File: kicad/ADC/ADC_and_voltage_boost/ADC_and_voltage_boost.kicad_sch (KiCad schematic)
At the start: 10 parts, among them J4 Screw_Terminal_01x02, U3 MOUDLE-SEEEDUINO-XIAO-ESP32C3, U4 MAX1032BEUG_

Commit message: finished schema/pcb
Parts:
- removed C10, C12, C7: 0.1e-6, Capacitor_SMD:C_1206_3216Metric_Pad1.33x1.80mm_HandSolder, symbol Device:C
- removed VoltageBoost1: TPS61023, TerminalBlock_Phoenix:TerminalBlock_Phoenix_MPT-0,5-4-2.54_1x04_P2.54mm_Horizontal, symbol Connector:Screw_Terminal_01x04
- added C1, C2, C3: 0.1e-6, Capacitor_SMD:C_1206_3216Metric_Pad1.33x1.80mm_HandSolder, symbol Device:C
- added J1: Screw_Terminal_01x04, TerminalBlock_Phoenix:TerminalBlock_Phoenix_MPT-0,5-4-2.54_1x04_P2.54mm_Horizontal, symbol Connector:Screw_Terminal_01x04
- J4: footprint (none) -> TerminalBlock_Phoenix:TerminalBlock_Phoenix_MPT-0,5-2-2.54_1x02_P2.54mm_Horizontal
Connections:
- net +3.3V: now also U4.17 (DVDD0), C3.1, J1.1 (Pin_1), J1.4 (Pin_4); no longer C11.1, C11.2, C8.1, C9.1, U3.13 (GND), U4.15 (DGND0), U4.16 (DGND), U4.2 (CH0), U4.21 (AGND3), U4.22 (AVDD2), U4.23 (AGND2), U4.24 (AGND1)
- net +5V: now reaches U4.1 (AVDD1)
- net +5V: now also C11.1, U4.18 (DVDD), U4.2 (CH0), U4.22 (AVDD2), C1.1, C2.1, J1.3 (Pin_3)
- new net GND: C1.2, C11.2, C2.2, C3.2, C8.1, C9.1, J1.2 (Pin_2), U3.13 (GND), U4.15 (DGND0), U4.16 (DGND), U4.21 (AGND3), U4.23 (AGND2), U4.24 (AGND1)
- no-connect marks 0 -> 12

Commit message: updated pcb
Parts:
- removed J4: Screw_Terminal_01x02, TerminalBlock_Phoenix:TerminalBlock_Phoenix_MPT-0,5-2-2.54_1x02_P2.54mm_Horizontal, symbol Connector:Screw_Terminal_01x02
- added J2: Screw_Terminal_01x04, TerminalBlock_Phoenix:TerminalBlock_Phoenix_MPT-0,5-4-2.54_1x04_P2.54mm_Horizontal, symbol Connector:Screw_Terminal_01x04
- C1, C11, C2, C3, C8, C9: footprint Capacitor_SMD:C_1206_3216Metric_Pad1.33x1.80mm_HandSolder -> Capacitor_SMD:C_0805_2012Metric
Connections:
- net GND: now also J2.2 (Pin_2), J2.4 (Pin_4)
- net at U4.3 (CH1): now also J2.3 (Pin_3)
- net at U4.4 (CH2): now also J2.1 (Pin_1)
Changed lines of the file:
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@@
+	)
+	(junction
+		(at 88.9 118.11)
+		(diameter 0)
+		(color 0 0 0 0)
 	)
 	(junction
@@
 	(wire
 		(pts
+			(xy 83.82 118.11) (xy 88.9 118.11)
+		)
+		(stroke
+			(width 0)
+			(type default)
+		)
+	)
+	(wire
+		(pts
 			(xy 161.29 87.63) (xy 191.77 87.63)
 		)
@@
 	(wire
 		(pts
+			(xy 88.9 118.11) (xy 88.9 127)
+		)
+		(stroke
+			(width 0)
+			(type default)
+		)
+	)
+	(wire
+		(pts
 			(xy 119.38 85.09) (xy 116.84 85.09)
 		)
@@
 	(wire
 		(pts
+			(xy 83.82 115.57) (xy 92.71 115.57)
+		)
+		(stroke
+			(width 0)
+			(type default)
+		)
+	)
+	(wire
+		(pts
+			(xy 83.82 120.65) (xy 125.73 120.65)
+		)
+		(stroke
+			(width 0)
+			(type default)
+		)
+	)
+	(wire
+		(pts
 			(xy 113.03 110.49) (xy 113.03 33.02)
 		)
@@
 	(wire
 		(pts
-			(xy 125.73 120.65) (xy 92.71 120.65)
-		)
-		(stroke
-			(width 0)
-			(type default)
-		)
-	)
-	(wire
-		(pts
 			(xy 166.37 74.93) (xy 166.37 92.71)
 		)
@@
 	(wire
 		(pts
+			(xy 83.82 113.03) (xy 88.9 113.03)
+		)
+		(stroke
+			(width 0)
+			(type default)
+		)
+	)
+	(wire
+		(pts
 			(xy 125.73 118.11) (xy 92.71 118.11)
 		)
@@
 	(wire
 		(pts
+			(xy 92.71 118.11) (xy 92.71 115.57)
+		)
+		(stroke
+			(width 0)
+			(type default)
+		)
+	)
+	(wire
+		(pts
 			(xy 119.38 74.93) (xy 166.37 74.93)
+		)
+		(stroke
+			(width 0)
+			(type default)
+		)
+	)
+	(wire
+		(pts
+			(xy 88.9 113.03) (xy 88.9 118.11)
 		)
 		(stroke
@@
 			)
 		)
-		(property "Footprint" "Capacitor_SMD:C_1206_3216Metric_Pad1.33x1.80mm_HandSolder"
+		(property "Footprint" "Capacitor_SMD:C_0805_2012Metric"
 			(at 182.5752 97.79 0)
 			(effects
@@
 			)
 		)
-		(property "Footprint" "Capacitor_SMD:C_1206_3216Metric_Pad1.33x1.80mm_HandSolder"
+		(property "Footprint" "Capacitor_SMD:C_0805_2012Metric"
 			(at 119.6848 140.97 0)
 			(effects
@@
 	)
 	(symbol
+		(lib_id "Connector:Screw_Terminal_01x04")
+		(at 78.74 118.11 180)
+		(unit 1)
+		(exclude_from_sim no)
+		(in_bom yes)
+		(on_board yes)
+		(dnp no)
+		(fields_autoplaced yes)
+		(property "Reference" "J2"
+			(at 78.74 106.68 0)
+			(effects
+				(font
+					(size 1.27 1.27)
+				)
+			)
+		)
+		(property "Value" "Screw_Terminal_01x04"
+			(at 78.74 109.22 0)
+			(effects
+				(font
+					(size 1.27 1.27)
+				)
+			)
+		)
+		(property "Footprint" "TerminalBlock_Phoenix:TerminalBlock_Phoenix_MPT-0,5-4-2.54_1x04_P2.54mm_Horizontal"
+			(at 78.74 118.11 0)
+			(effects
+				(font
+					(size 1.27 1.27)
+				)
+				(hide yes)
+			)
+		)
+		(property "Datasheet" "~"
+			(at 78.74 118.11 0)
+			(effects
+				(font
+					(size 1.27 1.27)
+				)
+				(hide yes)
+			)
+		)
+		(property "Description" "Generic screw terminal, single row, 01x04, script generated (kicad-library-utils/schlib/autogen/connector/)"
+			(at 78.74 118.11 0)
+			(effects
+				(font
+					(size 1.27 1.27)
+				)
+				(hide yes)
+			)
+		)
+		(pin "1"
+		)
+		(pin "2"
+		)
+		(pin "3"
+		)
+		(pin "4"
+		)
+		(instances
+			(project "ADC_and_voltage_boost"
+				(path "/47c680de-131f-4b08-bf1d-2ba63acc97af"
+					(reference "J2")
+					(unit 1)
+				)
+			)
+		)
+	)
+	(symbol
 		(lib_id "power:+3.3V")
 		(at 176.53 40.64 0)
@@
 			)
 		)
-		(property "Footprint" "Capacitor_SMD:C_1206_3216Metric_Pad1.33x1.80mm_HandSolder"
+		(property "Footprint" "Capacitor_SMD:C_0805_2012Metric"
 			(at 204.1652 92.71 0)
 			(effects
@@
 			)
 		)
-		(property "Footprint" "Capacitor_SMD:C_1206_3216Metric_Pad1.33x1.80mm_HandSolder"
+		(property "Footprint" "Capacitor_SMD:C_0805_2012Metric"
 			(at 117.8052 92.71 0)
 			(effects
@@
 	)
 	(symbol
-		(lib_id "Connector:Screw_Terminal_01x02")
-		(at 87.63 120.65 180)
-		(unit 1)
-		(exclude_from_sim no)
-		(in_bom yes)
-		(on_board yes)
-		(dnp no)
-		(fields_autoplaced yes)
-		(property "Reference" "J4"
-			(at 87.63 111.76 0)
-			(effects
-				(font
-					(size 1.27 1.27)
-				)
-			)
-		)
-		(property "Value" "Screw_Terminal_01x02"
-			(at 87.63 114.3 0)
-			(effects
-				(font
-					(size 1.27 1.27)
-				)
-			)
-		)
-		(property "Footprint" "TerminalBlock_Phoenix:TerminalBlock_Phoenix_MPT-0,5-2-2.54_1x02_P2.54mm_Horizontal"
-			(at 87.63 120.65 0)
-			(effects
-				(font
-					(size 1.27 1.27)
-				)
-				(hide yes)
-			)
-		)
-		(property "Datasheet" "~"
-			(at 87.63 120.65 0)
-			(effects
-				(font
-					(size 1.27 1.27)
-				)
-				(hide yes)
-			)
-		)
-		(property "Description" "Generic screw terminal, single row, 01x02, script generated (kicad-library-utils/schlib/autogen/connector/)"
-			(at 87.63 120.65 0)
-			(effects
-				(font
-					(size 1.27 1.27)
-				)
-				(hide yes)
-			)
-		)
-		(pin "2"
-		)
-		(pin "1"
-		)
-		(instances
-			(project "ADC_and_voltage_boost"
-				(path "/47c680de-131f-4b08-bf1d-2ba63acc97af"
-					(reference "J4")
-					(unit 1)
-				)
-			)
-		)
-	)
-	(symbol
 		(lib_id "power:+5V")
 		(at 166.37 92.71 270)
@@
 	(symbol
 		(lib_id "power:GND")
+		(at 88.9 127 0)
+		(unit 1)
+		(exclude_from_sim no)
+		(in_bom yes)
+		(on_board yes)
+		(dnp no)
+		(fields_autoplaced yes)
+		(property "Reference" "#PWR012"
+			(at 88.9 133.35 0)
+			(effects
+				(font
+					(size 1.27 1.27)
+				)
+				(hide yes)
+			)
+		)
+		(property "Value" "GND"
+			(at 88.9 132.08 0)
+			(effects
+				(font
+					(size 1.27 1.27)
+				)
+			)
+		)
+		(property "Footprint" ""
+			(at 88.9 127 0)
+			(effects
+				(font
+					(size 1.27 1.27)
+				)
+				(hide yes)
+			)
+		)
+		(property "Datasheet" ""
+			(at 88.9 127 0)
+			(effects
+				(font
+					(size 1.27 1.27)
+				)
+				(hide yes)
+			)
+		)
+		(property "Description" ""
+			(at 88.9 127 0)
+			(effects
+				(font
+					(size 1.27 1.27)
+				)
+			)
+		)
+		(pin "1"
+		)
+		(instances
+			(project "ADC_and_voltage_boost"
+				(path "/47c680de-131f-4b08-bf1d-2ba63acc97af"
+					(reference "#PWR012")
+					(unit 1)
+				)
+			)
+		)
+	)
+	(symbol
+		(lib_id "power:GND")
 		(at 116.84 92.71 0)
 		(unit 1)
@@
 			)
 		)
-		(property "Footprint" "Capacitor_SMD:C_1206_3216Metric_Pad1.33x1.80mm_HandSolder"
+		(property "Footprint" "Capacitor_SMD:C_0805_2012Metric"
 			(at 195.2752 97.79 0)
 			(effects
@@
 			)
 		)
-		(property "Footprint" "Capacitor_SMD:C_1206_3216Metric_Pad1.33x1.80mm_HandSolder"
+		(property "Footprint" "Capacitor_SMD:C_0805_2012Metric"
 			(at 122.2248 132.08 0)
 			(effects

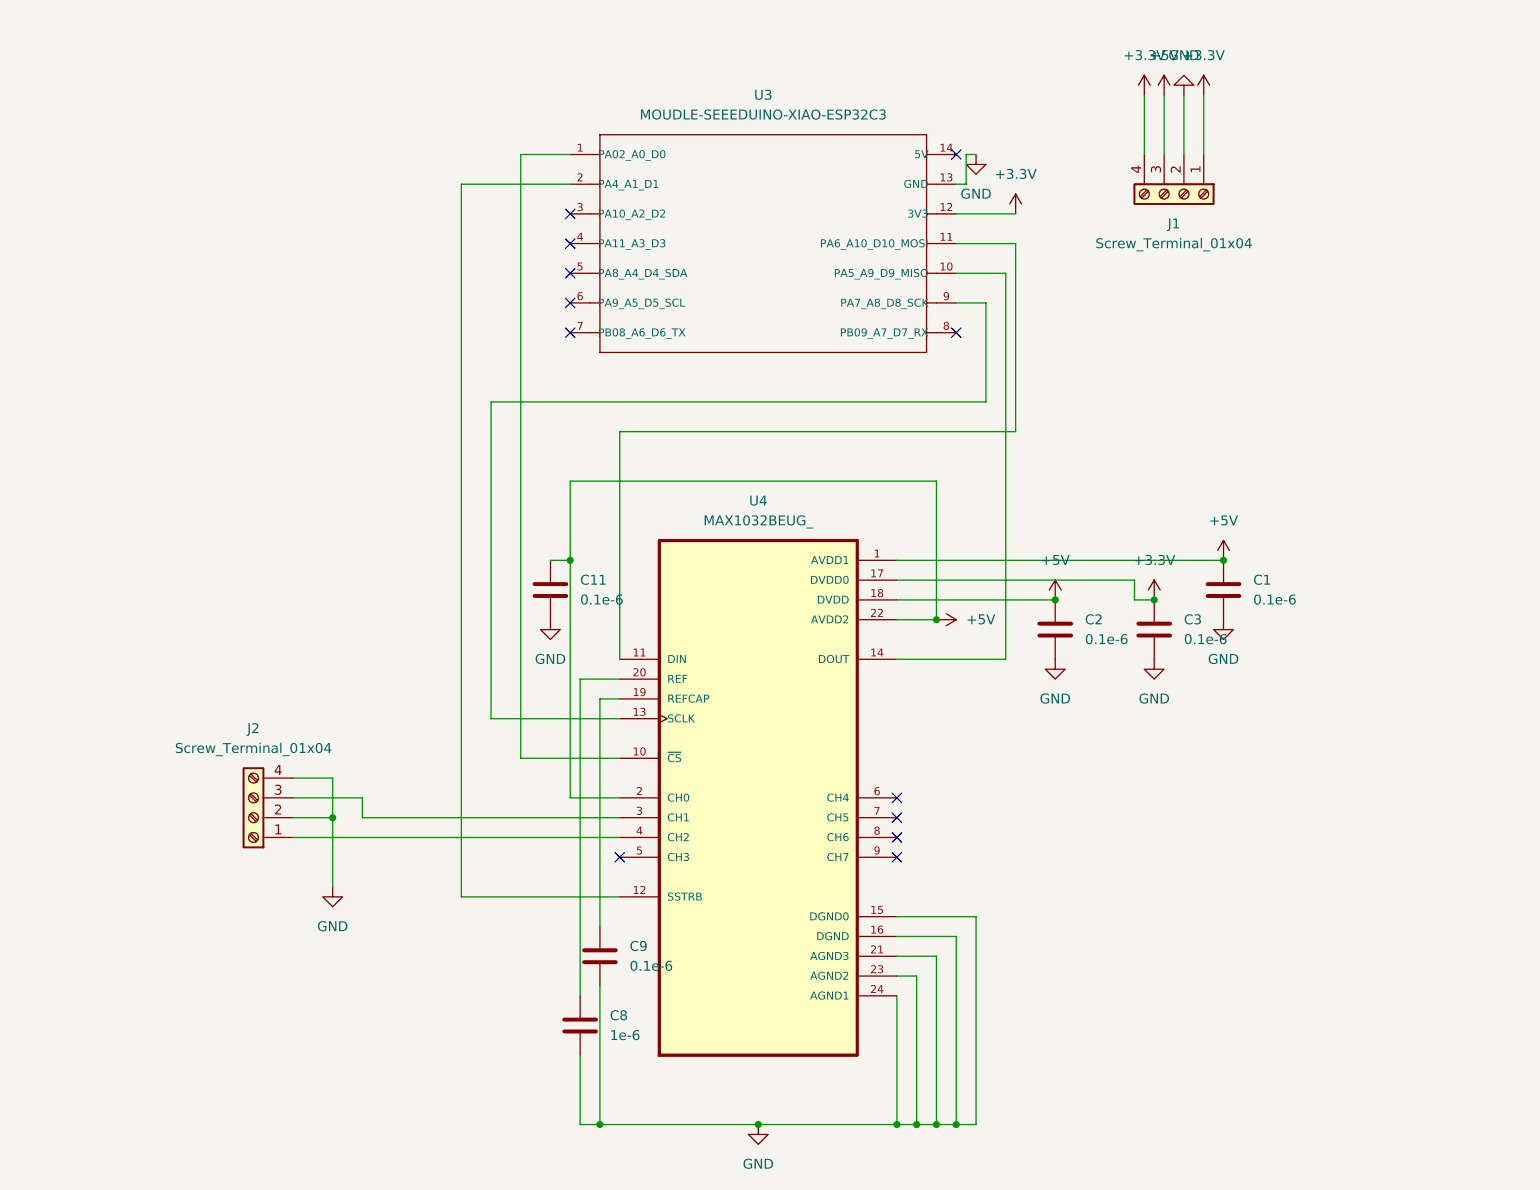
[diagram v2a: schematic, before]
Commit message: finished ADC
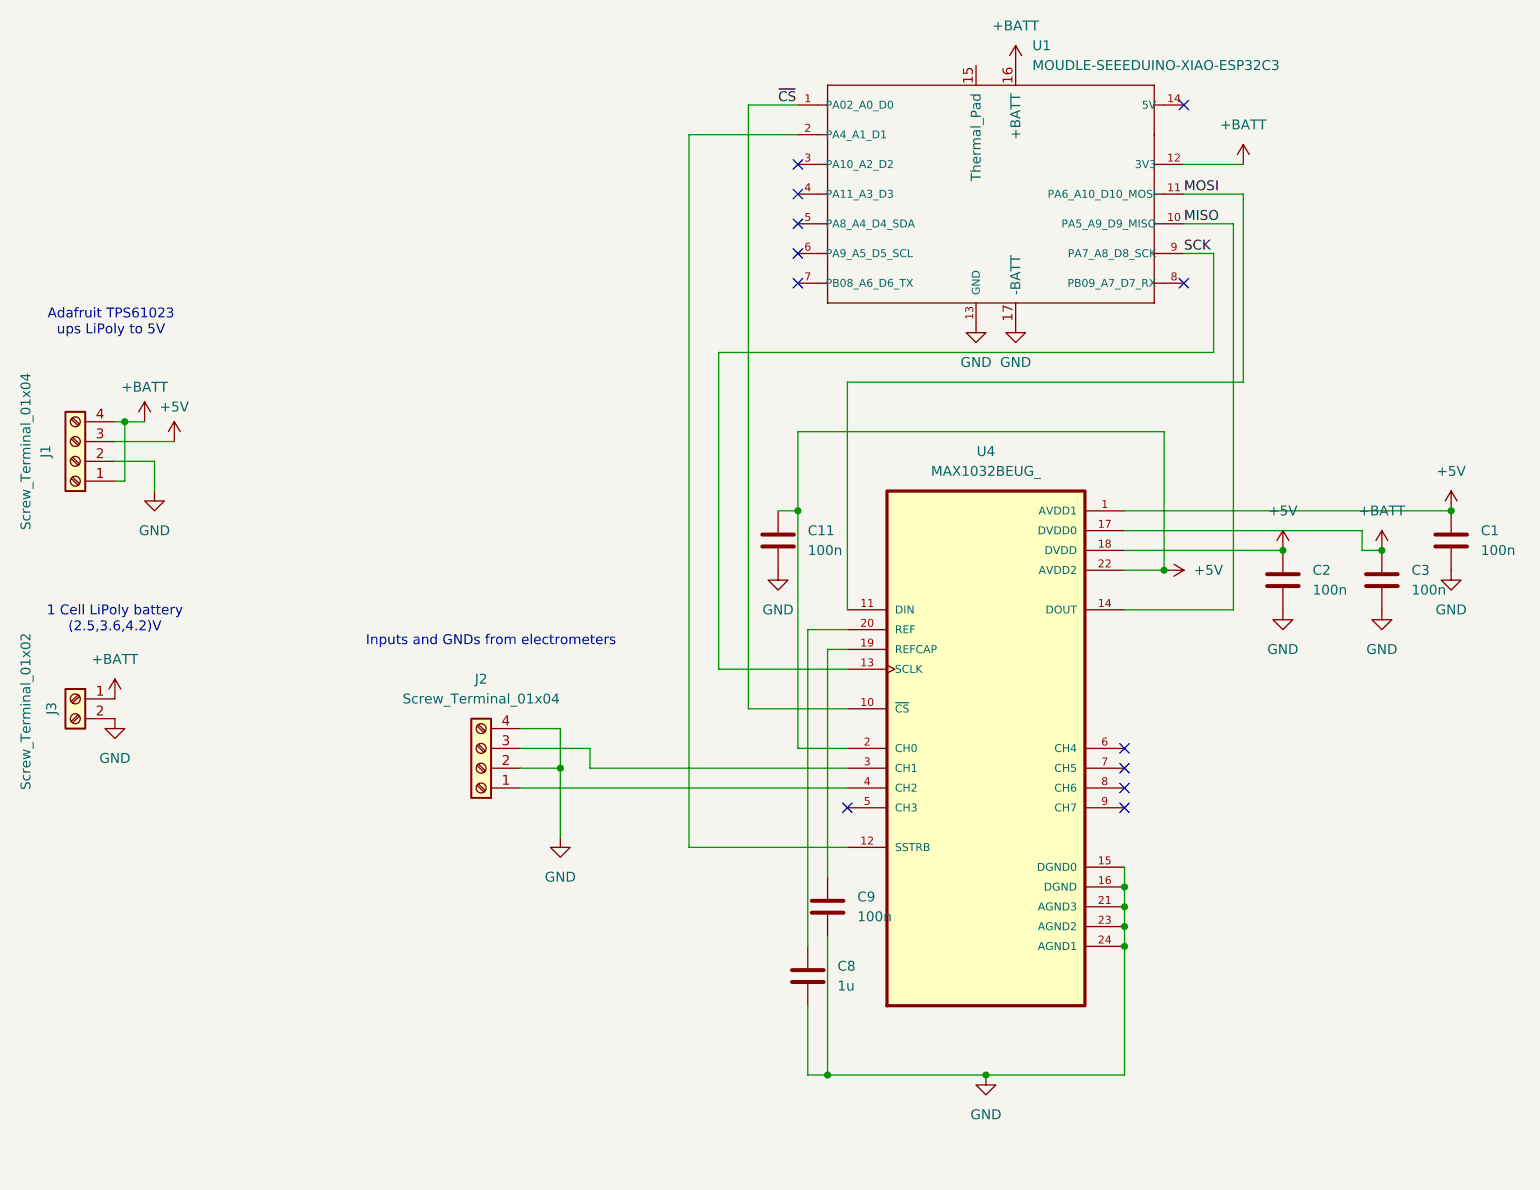
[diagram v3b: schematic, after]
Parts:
- removed U3: MOUDLE-SEEEDUINO-XIAO-ESP32C3, RF_Module:MCU_Seeed_ESP32C3, symbol XIAO-ESP32C3:MOUDLE-SEEEDUINO-XIAO-ESP32C3
- added J3: Screw_Terminal_01x02, Connector_PinHeader_2.54mm:PinHeader_1x02_P2.54mm_Vertical, symbol Connector:Screw_Terminal_01x02
- added U1: MOUDLE-SEEEDUINO-XIAO-ESP32C3, MOUDLE14P-SMD-2.54-21X17.8MM, symbol XIAO-ESP32C3:MOUDLE-SEEEDUINO-XIAO-ESP32C3
- C1, C11, C2, C3, C9: value 0.1e-6 -> 100n
- C8: value 1e-6 -> 1u
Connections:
- net GND: now also J3.2 (Pin_2), U1.13 (GND), U1.17 (-BATT)
- net ~{CS}: now reaches U4.10 (~{CS})
- net ~{CS}: now also U1.1 (PA02_A0_D0)
- net MOSI: now reaches U4.11 (DIN)
- net MOSI: now also U1.11 (PA6_A10_D10_MOSI)
- net at U4.12 (SSTRB): now also U1.2 (PA4_A1_D1)
- net SCK: now reaches U4.13 (SCLK)
- net SCK: now also U1.9 (PA7_A8_D8_SCK)
- net MISO: now reaches U4.14 (DOUT)
- net MISO: now also U1.10 (PA5_A9_D9_MISO)
- net +3.3V renamed +BATT
- net +BATT: now also J3.1 (Pin_1), U1.12 (3V3), U1.16 (+BATT)
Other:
- note added: "1 Cell LiPoly battery (2.5,3.6,4.2)V"
- note added: "Adafruit TPS61023 ups LiPoly to 5V"
- note added: "Inputs and GNDs from electrometers"
- company: (none) -> Coffee and Tellisense Lab
- title: (none) -> Electrometer ADC
- moved on the sheet: C1, C11, C2, C3, C8, C9, J1, J2, U4
